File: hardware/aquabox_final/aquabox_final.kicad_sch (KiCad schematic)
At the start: 0 parts

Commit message: Inicio do esquemático
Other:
- added sheet Display (Display.kicad_sch)
- added sheet ESP32_S3 (esp32_s3.kicad_sch)
- added sheet Expansion (expansion.kicad_sch)
- added sheet Inputs (inputs.kicad_sch)
- added sheet Power (power.kicad_sch)
- added sheet Pump_Relay (pump_relay.kicad_sch)
- added sheet RTC_SD (rtc_sd.kicad_sch)
- added sheet Solenoids (solenoids.kicad_sch)
- company: (none) -> Invenctus Soluções Tecnológicas
- title: (none) -> AQUABOX II

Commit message: Atualização
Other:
- removed sheet Display
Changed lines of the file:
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@@
 	)
 	(sheet
-		(at 127 140.97)
+		(at 195.58 110.49)
 		(size 34.29 13.97)
 		(exclude_from_sim no)
@@
 		)
 		(property "Sheetname" "Expansion"
-			(at 127 140.2584 0)
+			(at 195.58 109.7784 0)
 			(show_name no)
 			(do_not_autoplace no)
@@
 		)
 		(property "Sheetfile" "expansion.kicad_sch"
-			(at 127 155.5246 0)
+			(at 195.58 125.0446 0)
 			(show_name no)
 			(do_not_autoplace no)
@@
 	)
 	(sheet
-		(at 195.58 82.55)
+		(at 195.58 52.07)
 		(size 30.48 16.51)
 		(exclude_from_sim no)
@@
 		)
 		(property "Sheetname" "Pump_Relay"
-			(at 195.58 81.8384 0)
+			(at 195.58 51.3584 0)
 			(show_name no)
 			(do_not_autoplace no)
@@
 		)
 		(property "Sheetfile" "pump_relay.kicad_sch"
-			(at 195.58 99.6446 0)
+			(at 195.58 69.1646 0)
 			(show_name no)
 			(do_not_autoplace no)
@@
 	)
 	(sheet
-		(at 194.31 49.53)
-		(size 30.48 15.24)
-		(exclude_from_sim no)
-		(in_bom yes)
-		(on_board yes)
-		(dnp no)
-		(fields_autoplaced yes)
-		(stroke
-			(width 0.1524)
-			(type solid)
-		)
-		(fill
-			(color 0 0 0 0)
-		)
-		(property "Sheetname" "Display"
-			(at 194.31 48.8184 0)
-			(show_name no)
-			(do_not_autoplace no)
-			(effects
-				(font
-					(size 1.27 1.27)
-				)
-				(justify left bottom)
-			)
-		)
-		(property "Sheetfile" "Display.kicad_sch"
-			(at 194.31 65.3546 0)
-			(show_name no)
-			(do_not_autoplace no)
-			(effects
-				(font
-					(size 1.27 1.27)
-				)
-				(justify left top)
-			)
-		)
-		(instances
-			(project "aquabox_final"
-				(path "/c895ac8d-c639-4fea-ba83-739985d9c75e"
-					(page "4")
-				)
-			)
-		)
-	)
-	(sheet
-		(at 195.58 113.03)
+		(at 195.58 82.55)
 		(size 31.75 15.24)
 		(exclude_from_sim no)
@@
 		)
 		(property "Sheetname" "Solenoids"
-			(at 195.58 112.3184 0)
+			(at 195.58 81.8384 0)
 			(show_name no)
 			(do_not_autoplace no)
@@
 		)
 		(property "Sheetfile" "solenoids.kicad_sch"
-			(at 195.58 128.8546 0)
+			(at 195.58 98.3746 0)
 			(show_name no)
 			(do_not_autoplace no)

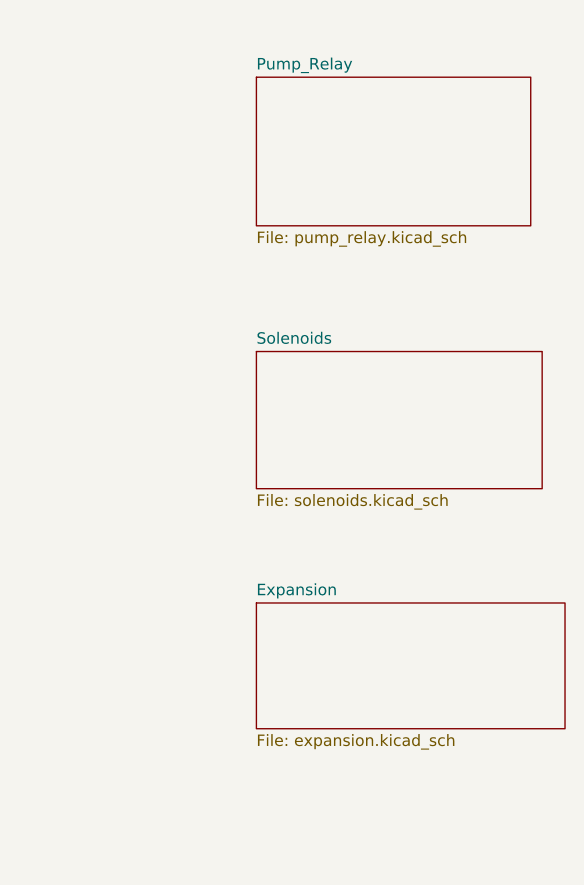
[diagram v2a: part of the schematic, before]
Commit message: Acionamento da bom e solenóides
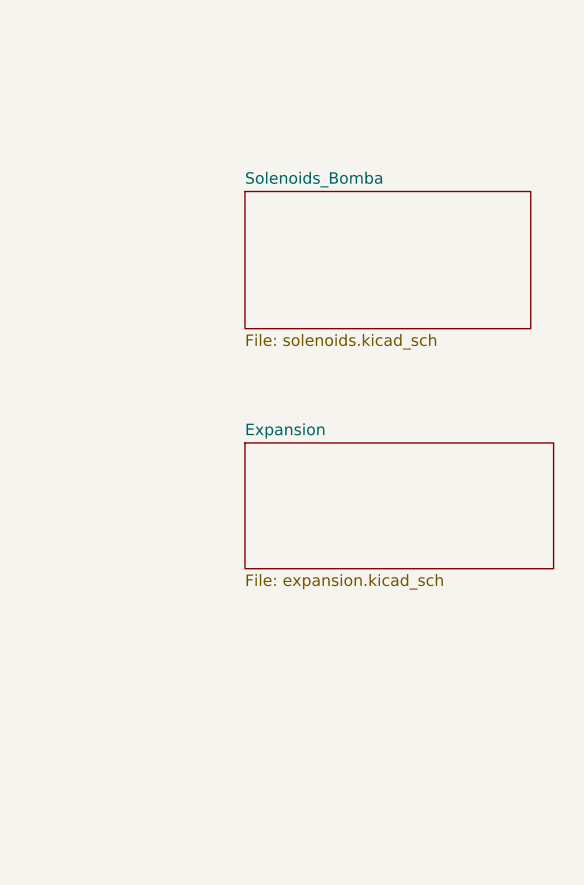
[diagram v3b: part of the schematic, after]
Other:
- sheet Solenoids renamed Solenoids_Bomba
- removed sheet Pump_Relay
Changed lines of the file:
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@@
 	)
 	(sheet
-		(at 195.58 110.49)
+		(at 194.31 92.71)
 		(size 34.29 13.97)
 		(exclude_from_sim no)
@@
 		)
 		(property "Sheetname" "Expansion"
-			(at 195.58 109.7784 0)
+			(at 194.31 91.9984 0)
 			(show_name no)
 			(do_not_autoplace no)
@@
 		)
 		(property "Sheetfile" "expansion.kicad_sch"
-			(at 195.58 125.0446 0)
+			(at 194.31 107.2646 0)
 			(show_name no)
 			(do_not_autoplace no)
@@
 	)
 	(sheet
-		(at 195.58 52.07)
-		(size 30.48 16.51)
-		(exclude_from_sim no)
-		(in_bom yes)
-		(on_board yes)
-		(dnp no)
-		(fields_autoplaced yes)
-		(stroke
-			(width 0.1524)
-			(type solid)
-		)
-		(fill
-			(color 0 0 0 0)
-		)
-		(property "Sheetname" "Pump_Relay"
-			(at 195.58 51.3584 0)
-			(show_name no)
-			(do_not_autoplace no)
-			(effects
-				(font
-					(size 1.27 1.27)
-				)
-				(justify left bottom)
-			)
-		)
-		(property "Sheetfile" "pump_relay.kicad_sch"
-			(at 195.58 69.1646 0)
-			(show_name no)
-			(do_not_autoplace no)
-			(effects
-				(font
-					(size 1.27 1.27)
-				)
-				(justify left top)
-			)
-		)
-		(instances
-			(project "aquabox_final"
-				(path "/c895ac8d-c639-4fea-ba83-739985d9c75e"
-					(page "7")
-				)
-			)
-		)
-	)
-	(sheet
-		(at 195.58 82.55)
+		(at 194.31 64.77)
 		(size 31.75 15.24)
 		(exclude_from_sim no)
@@
 			(color 0 0 0 0)
 		)
-		(property "Sheetname" "Solenoids"
-			(at 195.58 81.8384 0)
+		(property "Sheetname" "Solenoids_Bomba"
+			(at 194.31 64.0584 0)
 			(show_name no)
 			(do_not_autoplace no)
@@
 		)
 		(property "Sheetfile" "solenoids.kicad_sch"
-			(at 195.58 98.3746 0)
+			(at 194.31 80.5946 0)
 			(show_name no)
 			(do_not_autoplace no)
